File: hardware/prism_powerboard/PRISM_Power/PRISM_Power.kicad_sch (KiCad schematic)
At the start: 0 parts

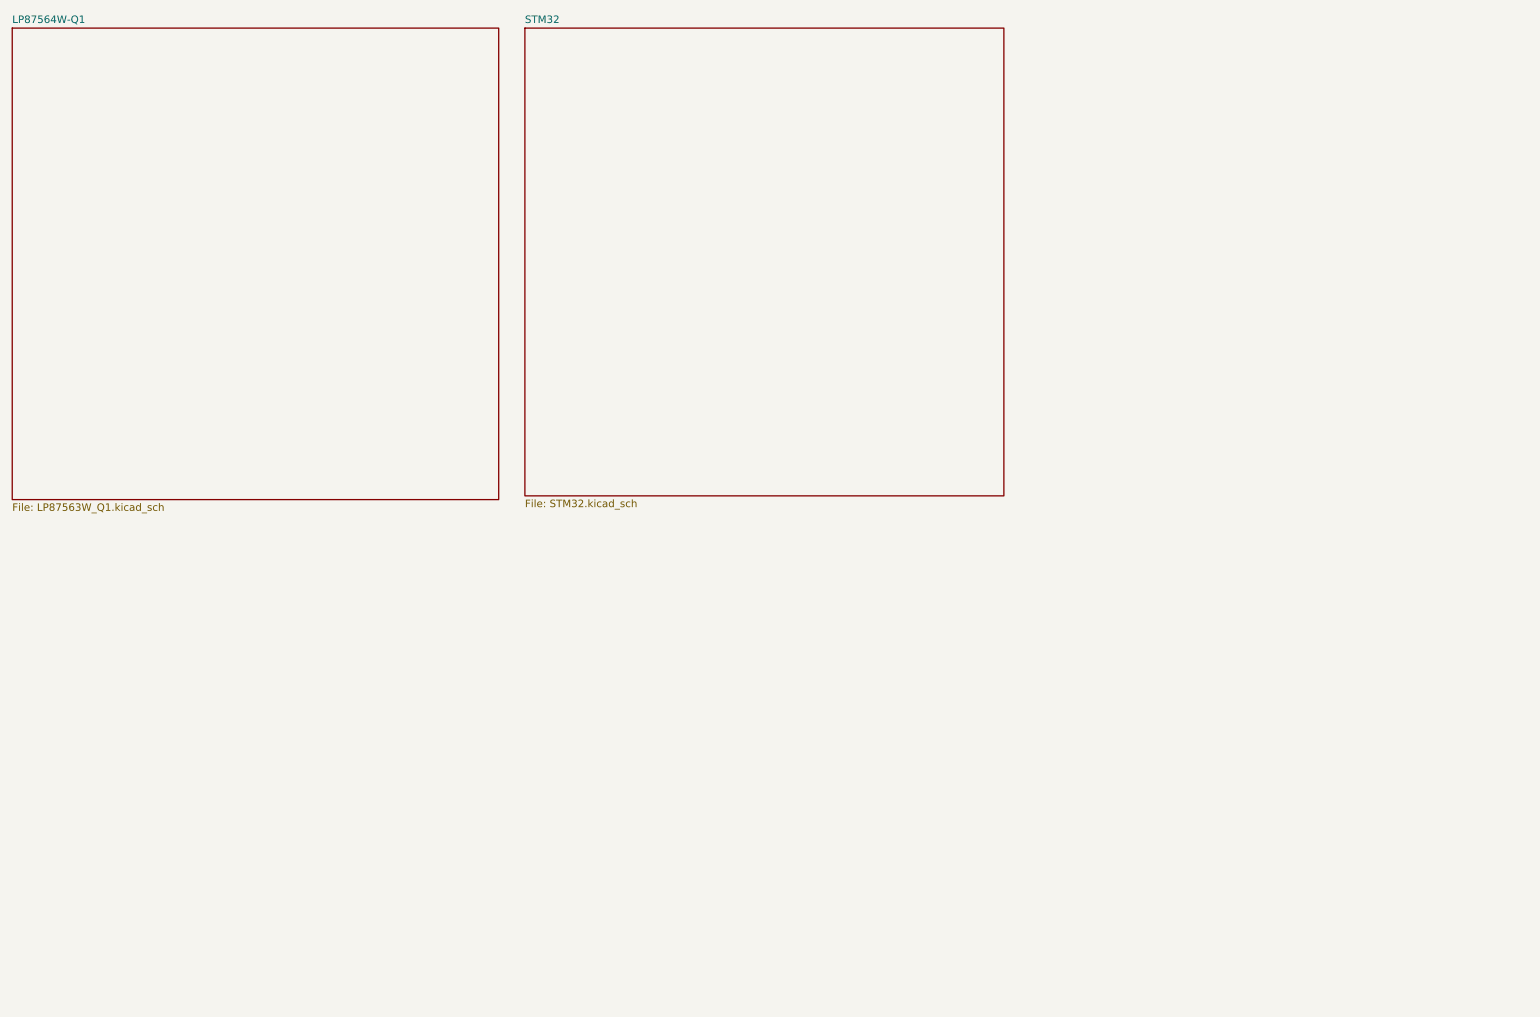
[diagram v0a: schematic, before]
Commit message: Power System Schematic
Large Updates to the Schematic, got BQ895, MAX1708, and BQ2970 almost finished. Need to work on LP87 now
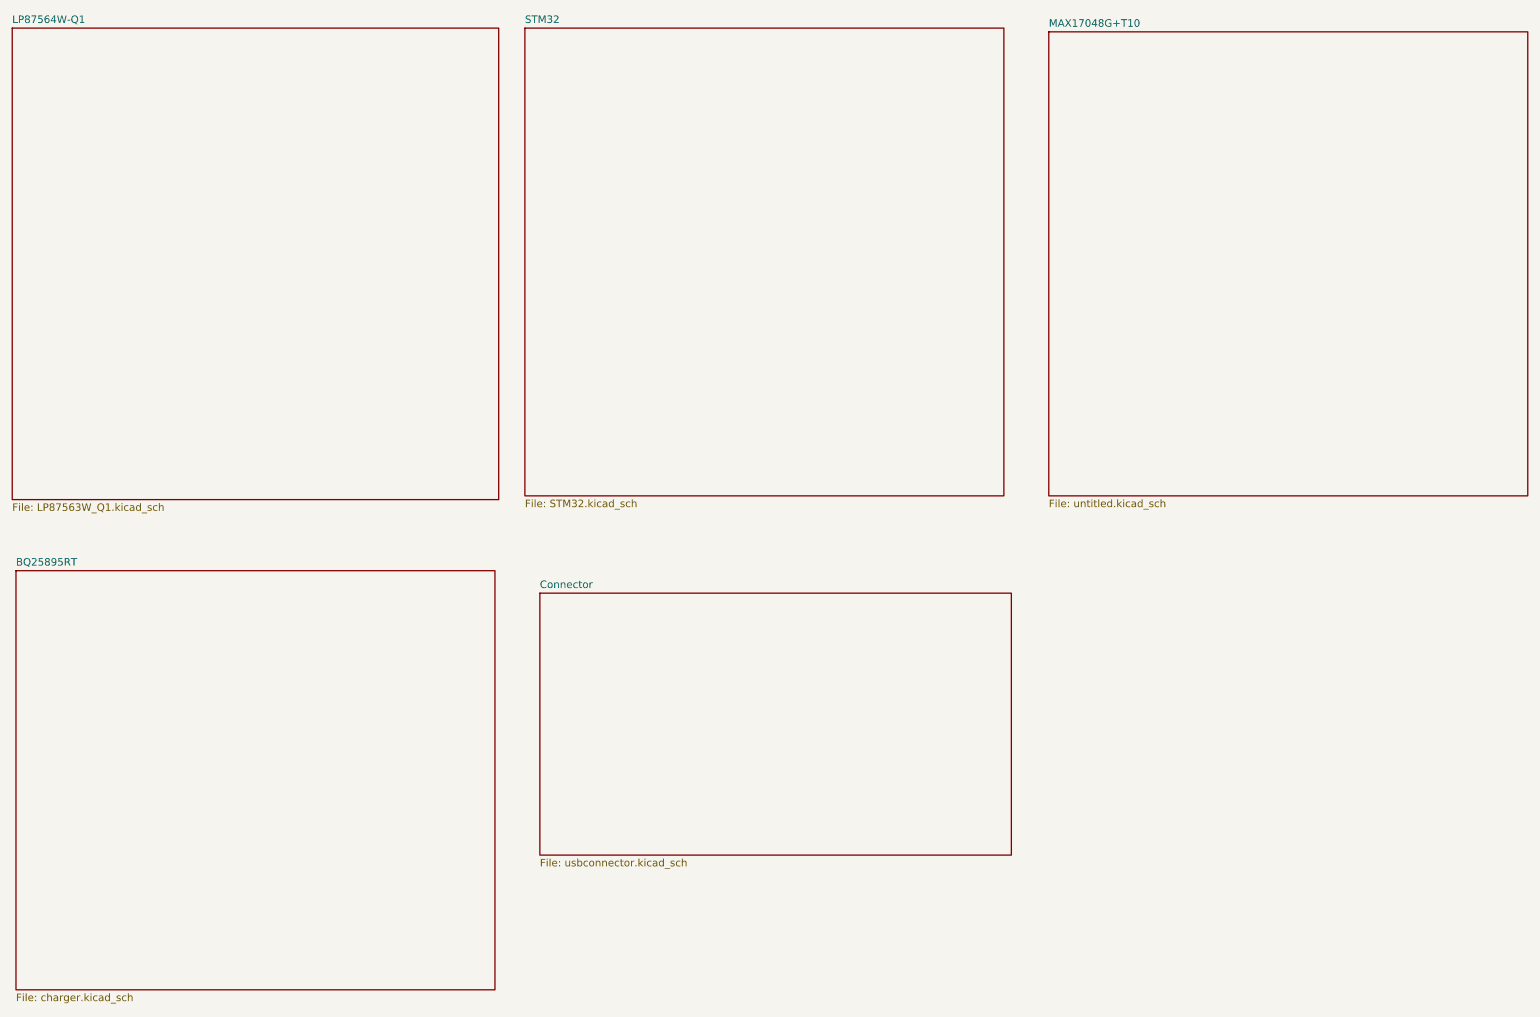
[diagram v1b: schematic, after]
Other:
- added sheet BQ25895RT (charger.kicad_sch)
- added sheet Connector (usbconnector.kicad_sch)
- added sheet MAX17048G+T10 (untitled.kicad_sch)
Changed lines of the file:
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@@
+	)
+	(sheet
+		(at 21.59 111.76)
+		(size 81.28 71.12)
+		(exclude_from_sim no)
+		(in_bom yes)
+		(on_board yes)
+		(dnp no)
+		(fields_autoplaced yes)
+		(stroke
+			(width 0.1524)
+			(type solid)
+		)
+		(fill
+			(color 0 0 0 0)
+		)
+		(property "Sheetname" "BQ25895RT"
+			(at 21.59 111.0484 0)
+			(show_name no)
+			(do_not_autoplace no)
+			(effects
+				(font
+					(size 1.27 1.27)
+				)
+				(justify left bottom)
+			)
+		)
+		(property "Sheetfile" "charger.kicad_sch"
+			(at 21.59 183.4646 0)
+			(show_name no)
+			(do_not_autoplace no)
+			(effects
+				(font
+					(size 1.27 1.27)
+				)
+				(justify left top)
+			)
+		)
+		(instances
+			(project "PRISM_Power"
+				(path "/80548bcf-507c-4ded-a0d2-b94774a2c706"
+					(page "5")
+				)
+			)
+		)
 	)
 	(sheet
@@
 				)
 			)
+		)
+	)
+	(sheet
+		(at 110.49 115.57)
+		(size 80.01 44.45)
+		(exclude_from_sim no)
+		(in_bom yes)
+		(on_board yes)
+		(dnp no)
+		(fields_autoplaced yes)
+		(stroke
+			(width 0.1524)
+			(type solid)
+		)
+		(fill
+			(color 0 0 0 0)
+		)
+		(property "Sheetname" "Connector"
+			(at 110.49 114.8584 0)
+			(show_name no)
+			(do_not_autoplace no)
+			(effects
+				(font
+					(size 1.27 1.27)
+				)
+				(justify left bottom)
+			)
+		)
+		(property "Sheetfile" "usbconnector.kicad_sch"
+			(at 110.49 160.6046 0)
+			(show_name no)
+			(do_not_autoplace no)
+			(effects
+				(font
+					(size 1.27 1.27)
+				)
+				(justify left top)
+			)
+		)
+		(instances
+			(project "PRISM_Power"
+				(path "/80548bcf-507c-4ded-a0d2-b94774a2c706"
+					(page "6")
+				)
+			)
+		)
+	)
+	(sheet
+		(at 196.85 20.32)
+		(size 81.28 78.74)
+		(exclude_from_sim no)
+		(in_bom yes)
+		(on_board yes)
+		(dnp no)
+		(fields_autoplaced yes)
+		(stroke
+			(width 0.1524)
+			(type solid)
+		)
+		(fill
+			(color 0 0 0 0)
+		)
+		(property "Sheetname" "MAX17048G+T10"
+			(at 196.85 19.6084 0)
+			(show_name no)
+			(do_not_autoplace no)
+			(effects
+				(font
+					(size 1.27 1.27)
+				)
+				(justify left bottom)
+			)
+		)
+		(property "Sheetfile" "untitled.kicad_sch"
+			(at 196.85 99.6446 0)
+			(show_name no)
+			(do_not_autoplace no)
+			(effects
+				(font
+					(size 1.27 1.27)
+				)
+				(justify left top)
+			)
+		)
+		(instances
+			(project "PRISM_Power"
+				(path "/80548bcf-507c-4ded-a0d2-b94774a2c706"
+					(page "4")
+				)
+			)
